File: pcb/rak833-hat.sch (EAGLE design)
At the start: 8 parts, among them IC2 AMS1117-3.3, K1 PIN20X2

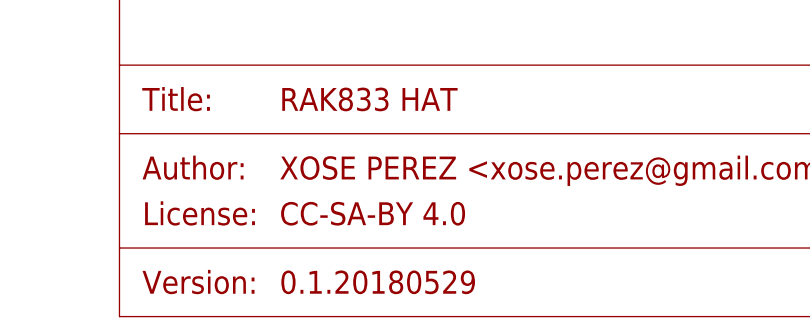
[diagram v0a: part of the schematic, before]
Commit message: Fixing switch footprint
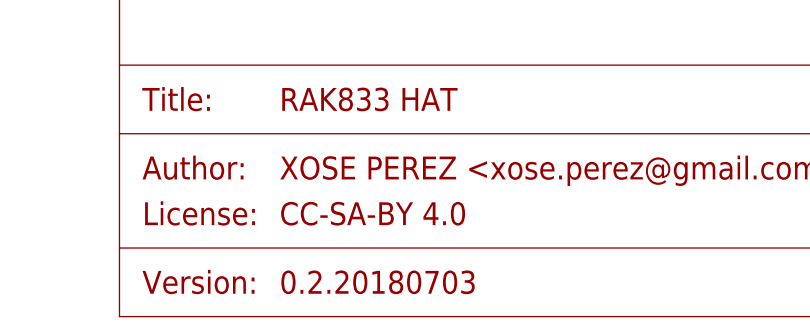
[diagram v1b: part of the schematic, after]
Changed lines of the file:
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@@
 <?xml version="1.0" encoding="utf-8"?>
 <!DOCTYPE eagle SYSTEM "eagle.dtd">
-<eagle version="8.7.0">
+<eagle version="9.0.1">
 <drawing>
 <settings>
@@
 <attribute name="PROJECT_LICENSE" value="CC-SA-BY 4.0"/>
 <attribute name="PROJECT_NAME" value="RAK833 HAT"/>
-<attribute name="PROJECT_VERSION" value="0.1.20180529"/>
+<attribute name="PROJECT_VERSION" value="0.2.20180703"/>
 </attributes>
 <variantdefs>
